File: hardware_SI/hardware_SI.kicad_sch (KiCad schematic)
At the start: 44 parts, among them J1 Conn_01x07_Female, J2 USB_B_Micro, J3 Jack-DC, Q1 Q_PMOS_GSD, Q2 Q_PMOS_GSD, SW1 SW_SPDT, U1 OMEGA2+, U2 MAX6369, U4 LTC4085EDEPBF, U5 TPS61200DRC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

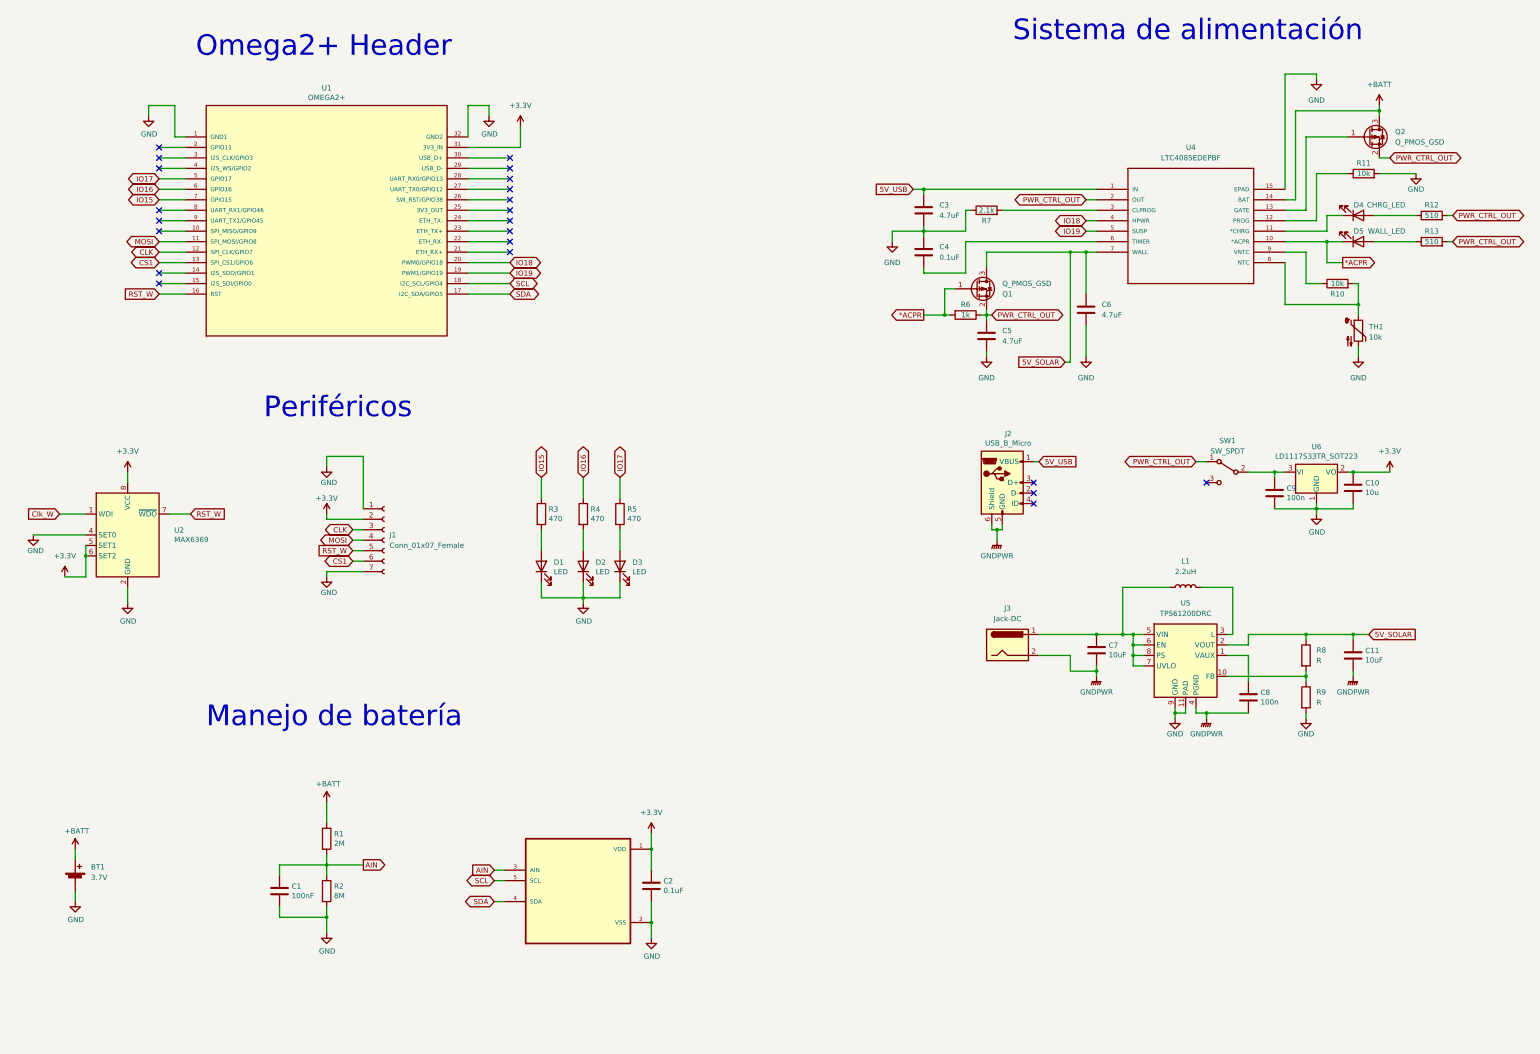
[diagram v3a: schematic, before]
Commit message: etiquetas y hojas jerárquicas
Agrupación de subsistemas en hojas jerárquicas y cambios de etiquetas globales por locales y jerárquicas
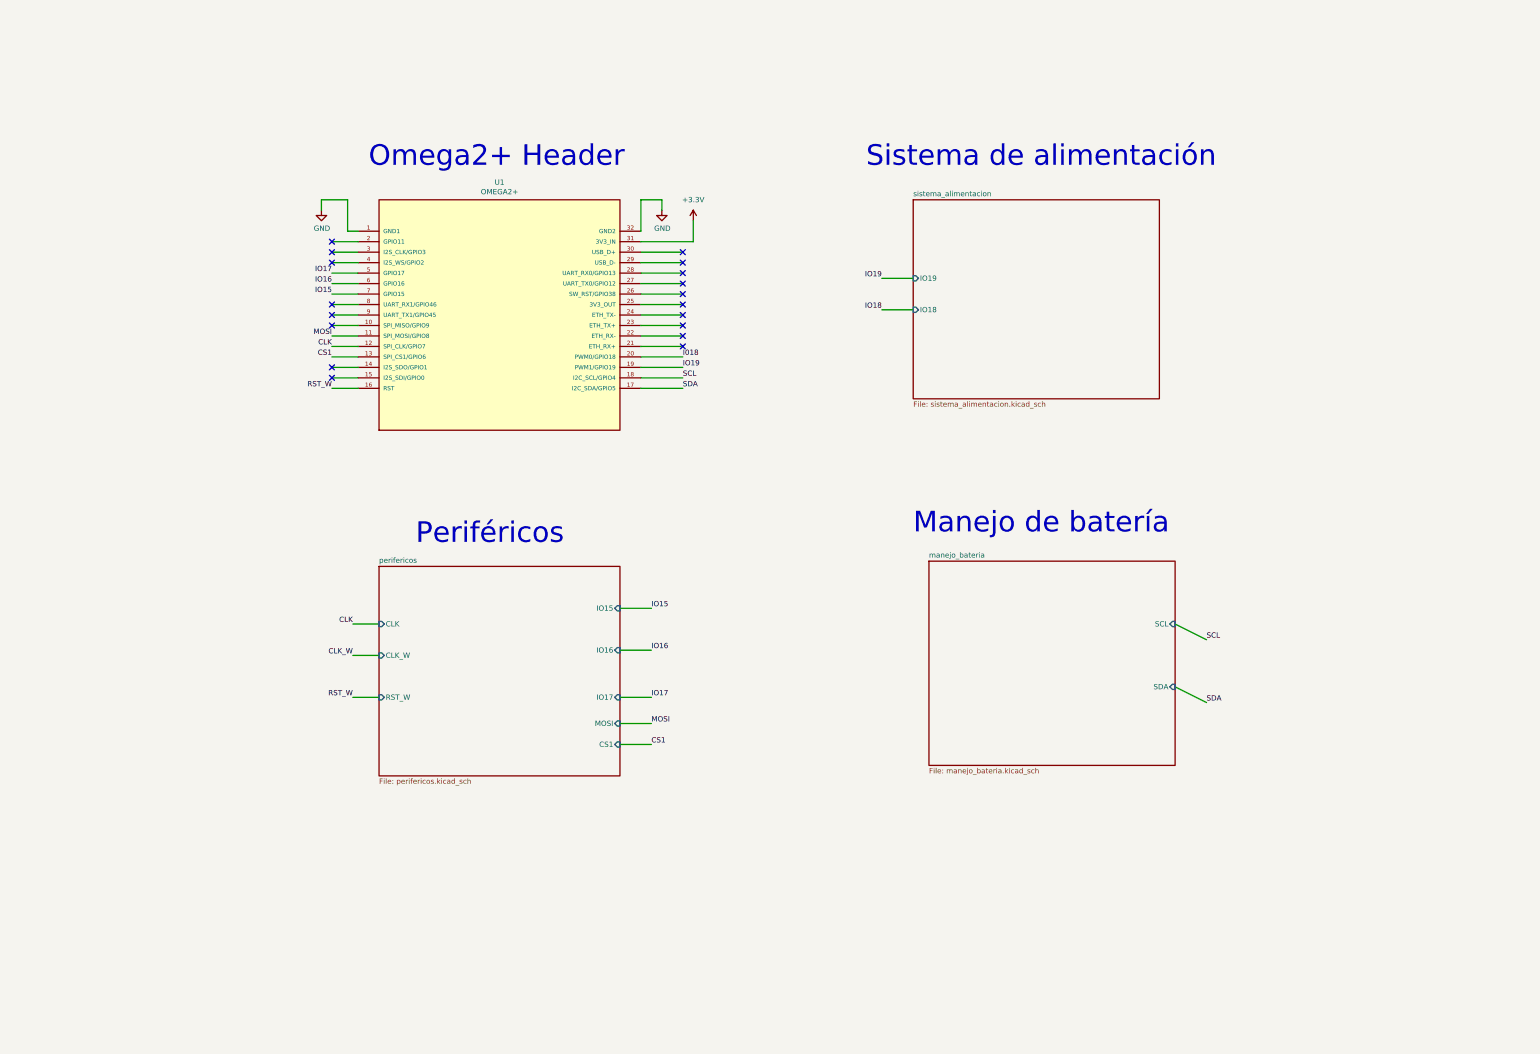
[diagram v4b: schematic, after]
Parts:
- removed BT1: 3.7V, Battery:BatteryHolder_MPD_BH-18650-PC2, symbol Device:Battery_Cell
- removed C1: 100nF, Capacitor_SMD:C_0805_2012Metric_Pad1.18x1.45mm_HandSolder, symbol Device:C
- removed C10: 10u, Capacitor_SMD:C_0805_2012Metric_Pad1.18x1.45mm_HandSolder, symbol Device:C
- removed C11, C7: 10uF, Capacitor_SMD:C_0805_2012Metric_Pad1.18x1.45mm_HandSolder, symbol Device:C
- removed C2, C4: 0.1uF, Capacitor_SMD:C_0805_2012Metric_Pad1.18x1.45mm_HandSolder, symbol Device:C
- removed C3, C5, C6: 4.7uF, Capacitor_SMD:C_0805_2012Metric_Pad1.18x1.45mm_HandSolder, symbol Device:C
- removed C8, C9: 100n, Capacitor_SMD:C_0805_2012Metric_Pad1.18x1.45mm_HandSolder, symbol Device:C
- removed D1, D2, D3: LED, LED_SMD:LED_0805_2012Metric_Pad1.15x1.40mm_HandSolder, symbol Device:LED
- removed D4: CHRG_LED, LED_SMD:LED_0805_2012Metric_Pad1.15x1.40mm_HandSolder, symbol Device:LED
- removed D5: WALL_LED, LED_SMD:LED_0805_2012Metric_Pad1.15x1.40mm_HandSolder, symbol Device:LED
- removed J1: Conn_01x07_Female, Connector_PinSocket_2.54mm:PinSocket_1x07_P2.54mm_Vertical, symbol Connector:Conn_01x07_Female
- removed J2: USB_B_Micro, Connector_USB:USB_Micro-B_Molex-105017-0001, symbol Connector:USB_B_Micro
- removed J3: Jack-DC, Connector_BarrelJack:BarrelJack_SwitchcraftConxall_RAPC10U_Horizontal, symbol Connector:Jack-DC
- removed L1: 2.2uH, Inductor_SMD:L_Coilcraft_LPS4018, symbol Device:L
- removed Q1, Q2: Q_PMOS_GSD, Package_TO_SOT_SMD:SOT-23_Handsoldering, symbol Device:Q_PMOS_GSD
- removed R1: 2M, Resistor_SMD:R_0805_2012Metric_Pad1.20x1.40mm_HandSolder, symbol Device:R
- removed R10, R11: 10k, Resistor_SMD:R_0805_2012Metric_Pad1.20x1.40mm_HandSolder, symbol Device:R
- removed R12, R13: 510, Resistor_SMD:R_0805_2012Metric_Pad1.20x1.40mm_HandSolder, symbol Device:R
- removed R2: 8M, Resistor_SMD:R_0805_2012Metric_Pad1.20x1.40mm_HandSolder, symbol Device:R
- removed R3, R4, R5: 470, Resistor_SMD:R_0805_2012Metric_Pad1.20x1.40mm_HandSolder, symbol Device:R
- removed R6: 1k, Resistor_SMD:R_0805_2012Metric_Pad1.20x1.40mm_HandSolder, symbol Device:R
- removed R7: 2.1k, Resistor_SMD:R_0805_2012Metric_Pad1.20x1.40mm_HandSolder, symbol Device:R
- removed R8, R9: R, Resistor_SMD:R_0805_2012Metric_Pad1.20x1.40mm_HandSolder, symbol Device:R
- removed SW1: SW_SPDT, Button_Switch_THT:SW_CuK_OS102011MA1QN1_SPDT_Angled, symbol Switch:SW_SPDT
- removed TH1: 10k, Resistor_SMD:R_0603_1608Metric_Pad0.98x0.95mm_HandSolder, symbol Device:Thermistor_NTC
- removed U2: MAX6369, Package_TO_SOT_SMD:SOT-23-8, symbol Power_Supervisor:MAX6369
- removed U3: (no value), SOT95P270X145-5N, symbol MCP3021A5T-E_OT:MCP3021A5T-E/OT
- removed U4: LTC4085EDEPBF, LTC4085EDEPBF:DFN-14_DE, symbol LTC4085EDEPBF:LTC4085EDEPBF
- removed U5: TPS61200DRC, Package_SON:Texas_S-PVSON-N10_ThermalVias, symbol Regulator_Switching:TPS61200DRC
- removed U6: LD1117S33TR_SOT223, Package_TO_SOT_SMD:SOT-223-3_TabPin2, symbol Regulator_Linear:LD1117S33TR_SOT223
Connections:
- net IO18: no longer U1.20 (PWM0/GPIO18)
- new net I018: U1.20 (PWM0/GPIO18)
- no-connect marks 22 -> 18
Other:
- added sheet manejo_bateria (manejo_bateria.kicad_sch)
- added sheet perifericos (perifericos.kicad_sch)
- added sheet sistema_alimentacion (sistema_alimentacion.kicad_sch)
- moved on the sheet: U1

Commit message: Etq compon, C desacop, ferrita
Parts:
- added C1: 100n, symbol Device:C
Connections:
- net +3V3: now also C1.1
- net GND: now also C1.2
